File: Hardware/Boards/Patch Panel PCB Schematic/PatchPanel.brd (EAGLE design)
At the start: 226 x 119 mm, 49 parts

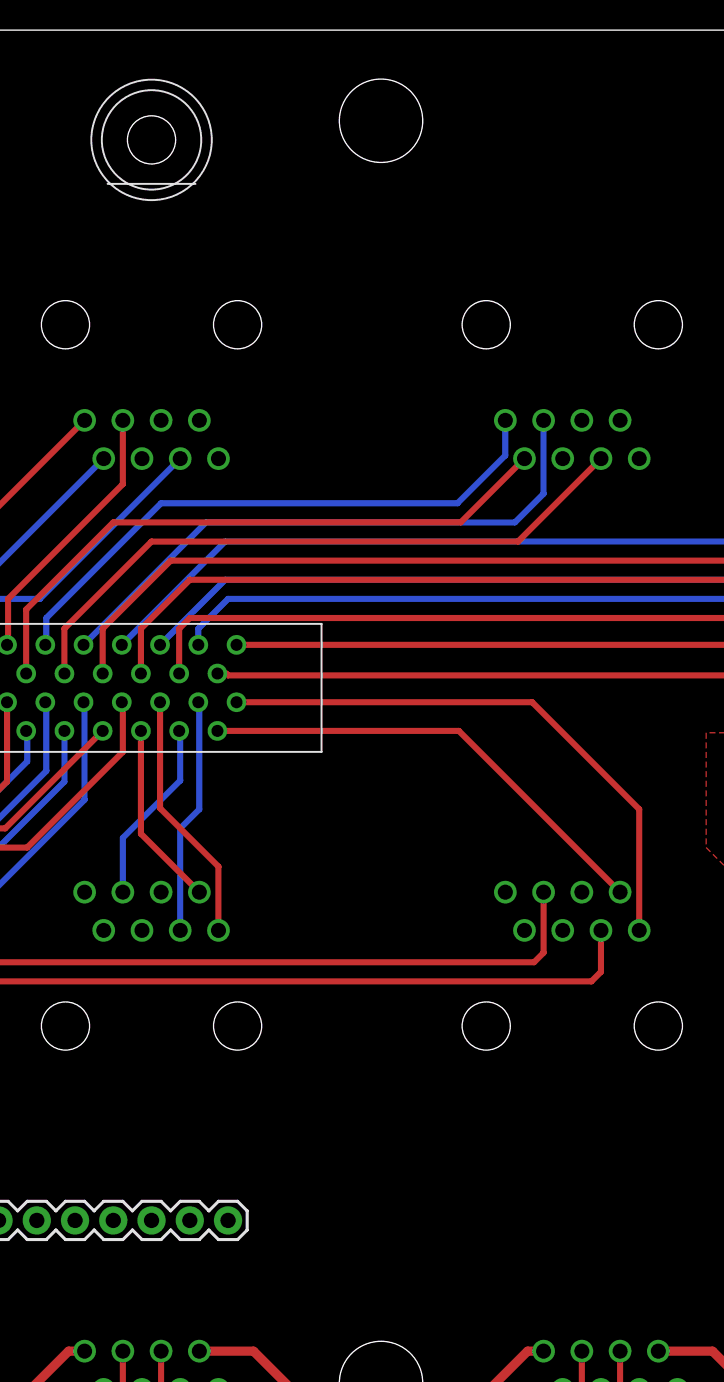
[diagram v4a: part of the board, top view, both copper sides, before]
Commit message: Moved SMA connector
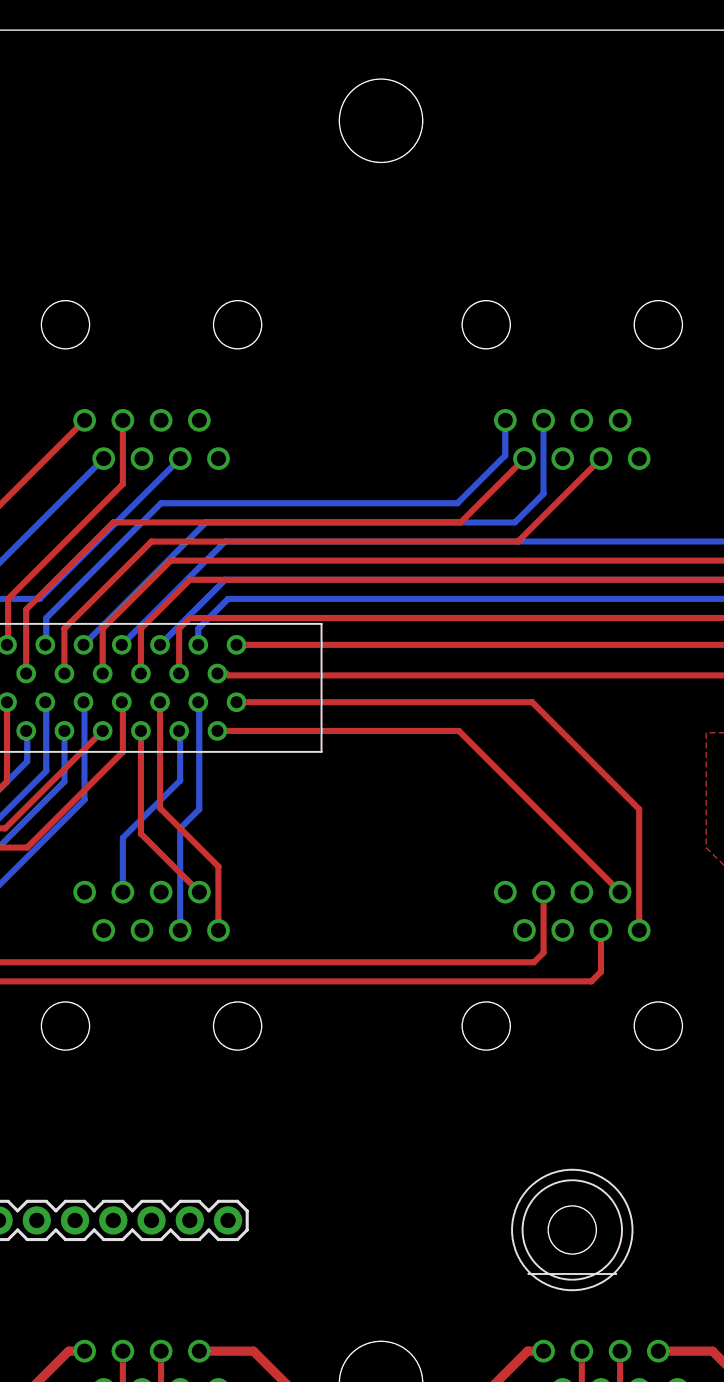
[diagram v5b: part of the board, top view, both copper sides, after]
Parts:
- moved U$16 77.6 mm to (154.9, 39.4)
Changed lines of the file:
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@@
 <element name="U$14" library="ant-pass-through" package="N-TYPE" value="N-TYPE-THRU" x="12.7" y="21.59"/>
 <element name="U$15" library="ant-pass-through" package="N-TYPE" value="N-TYPE-THRU" x="181.61" y="46.99"/>
-<element name="U$16" library="ant-pass-through" package="SMA" value="SMA-THRU" x="127" y="111.76"/>
+<element name="U$16" library="ant-pass-through" package="SMA" value="SMA-THRU" x="154.94" y="39.37"/>
 </elements>
 <signals>

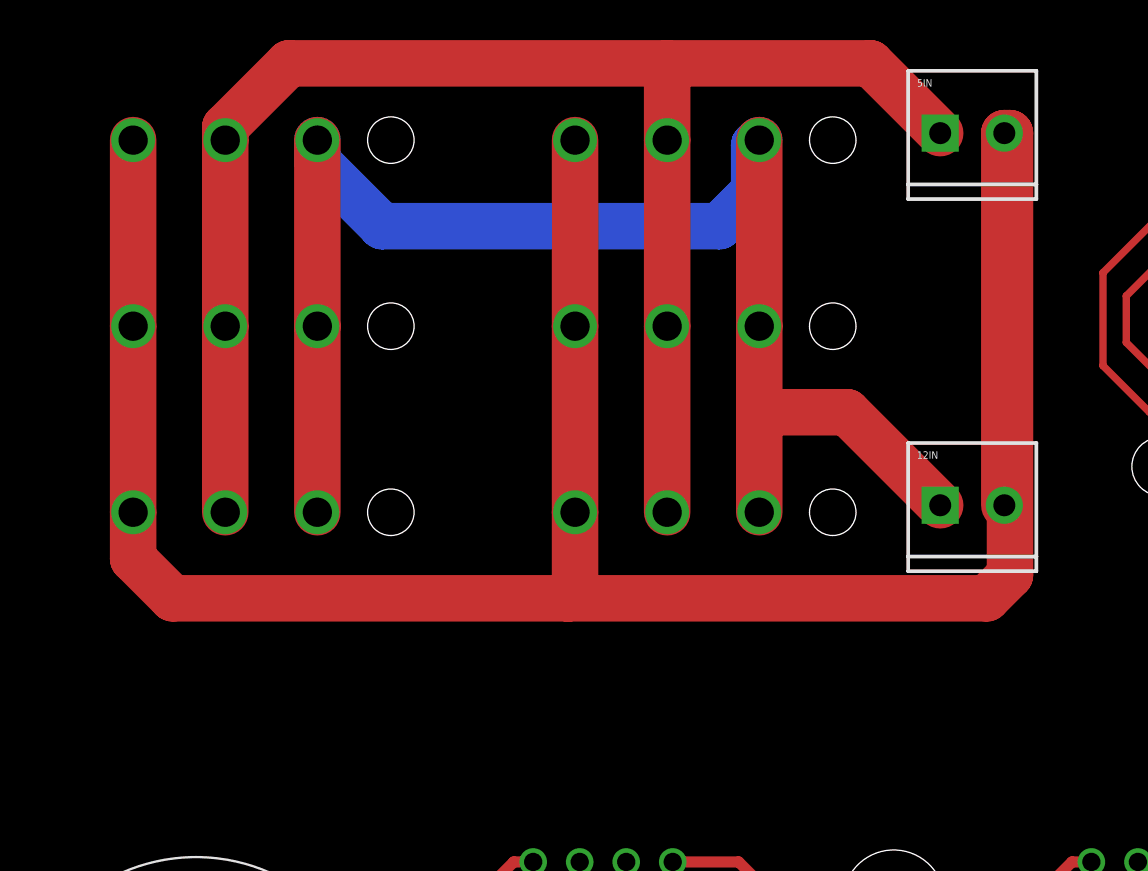
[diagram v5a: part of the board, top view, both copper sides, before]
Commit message: Added space between aux power connectors
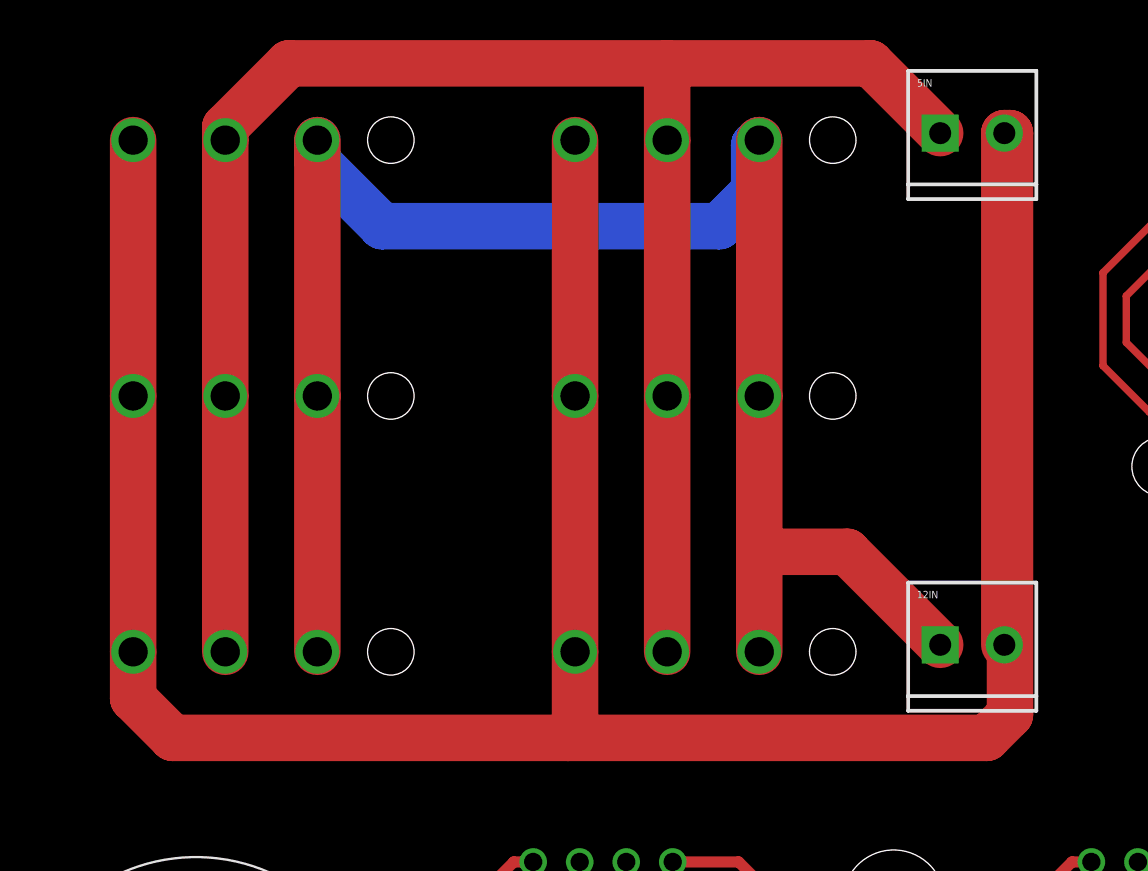
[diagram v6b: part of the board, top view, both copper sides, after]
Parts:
- moved 12IN 7.62 mm to (53.3, 43.2)
- moved U$6 7.62 mm to (5.08, 47.0)
- moved U$7 7.62 mm to (29.2, 47.0)
- moved U$4 3.81 mm to (5.08, 61.0)
- moved U$5 3.81 mm to (29.2, 61.0)
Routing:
- net GND: track 142.1 -> 172.6 mm
- net +5V: track 87.6 -> 102.8 mm
- net +12V: track 82.8 -> 98.0 mm
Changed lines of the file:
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@@
 <element name="RS-485_OUT7" library="PCB0M1" package="RJ45-CAT5E" value="RJ45" x="43.18" y="97.79" rot="MR180"/>
 <element name="U$1" library="harting-scsi" package="60050685100" value="TB60050685100" x="85.09" y="71.12"/>
-<element name="12IN" library="SparkFun-Connectors" package="SCREWTERMINAL-3.5MM-2" value="M023.5MM" x="53.34" y="50.8"/>
+<element name="12IN" library="SparkFun-Connectors" package="SCREWTERMINAL-3.5MM-2" value="M023.5MM" x="53.34" y="43.18"/>
 <element name="5IN" library="SparkFun-Connectors" package="SCREWTERMINAL-3.5MM-2" value="M023.5MM" x="53.34" y="71.12"/>
 <element name="U$2" library="molex-power" package="0.93&quot;" value="3PIN" x="5.08" y="74.93" rot="MR180"/>
 <element name="U$3" library="molex-power" package="0.93&quot;" value="3PIN" x="29.21" y="74.93" rot="MR180"/>
-<element name="U$4" library="molex-power" package="0.93&quot;" value="3PIN" x="5.08" y="64.77" rot="MR180"/>
-<element name="U$5" library="molex-power" package="0.93&quot;" value="3PIN" x="29.21" y="64.77" rot="MR180"/>
-<element name="U$6" library="molex-power" package="0.93&quot;" value="3PIN" x="5.08" y="54.61" rot="MR180"/>
-<element name="U$7" library="molex-power" package="0.93&quot;" value="3PIN" x="29.21" y="54.61" rot="MR180"/>
+<element name="U$4" library="molex-power" package="0.93&quot;" value="3PIN" x="5.08" y="60.96" rot="MR180"/>
+<element name="U$5" library="molex-power" package="0.93&quot;" value="3PIN" x="29.21" y="60.96" rot="MR180"/>
+<element name="U$6" library="molex-power" package="0.93&quot;" value="3PIN" x="5.08" y="46.99" rot="MR180"/>
+<element name="U$7" library="molex-power" package="0.93&quot;" value="3PIN" x="29.21" y="46.99" rot="MR180"/>
 <element name="U$8" library="MLX" package="42002-2" value="MLX-2" x="172.72" y="69.85" rot="MR0"/>
 <element name="U$9" library="MLX" package="42002-2" value="MLX-2" x="194.31" y="64.77" rot="R90"/>
@@
 <contactref element="U$7" pad="3"/>
 <contactref element="U$6" pad="3"/>
-<wire x1="9.271" y1="70.739" x2="9.271" y2="60.579" width="2.54" layer="1"/>
-<wire x1="9.271" y1="60.579" x2="9.271" y2="50.419" width="2.54" layer="1"/>
-<wire x1="33.401" y1="70.739" x2="33.401" y2="60.579" width="2.54" layer="1"/>
-<wire x1="33.401" y1="60.579" x2="33.401" y2="50.419" width="2.54" layer="1"/>
-<wire x1="56.84" y1="50.8" x2="56.84" y2="71.12" width="2.54" layer="1"/>
+<wire x1="9.271" y1="70.739" x2="9.271" y2="56.769" width="2.54" layer="1"/>
+<wire x1="9.271" y1="56.769" x2="9.271" y2="42.799" width="2.54" layer="1"/>
+<wire x1="33.401" y1="70.739" x2="33.401" y2="56.769" width="2.54" layer="1"/>
+<wire x1="33.401" y1="56.769" x2="33.401" y2="42.799" width="2.54" layer="1"/>
+<wire x1="56.84" y1="43.18" x2="56.84" y2="71.12" width="2.54" layer="1"/>
 <wire x1="56.84" y1="71.12" x2="57.15" y2="71.12" width="2.54" layer="1"/>
-<wire x1="57.15" y1="71.12" x2="57.15" y2="46.99" width="2.54" layer="1"/>
-<wire x1="57.15" y1="46.99" x2="55.88" y2="45.72" width="2.54" layer="1"/>
-<wire x1="55.88" y1="45.72" x2="33.02" y2="45.72" width="2.54" layer="1"/>
-<wire x1="11.43" y1="45.72" x2="9.271" y2="47.879" width="2.54" layer="1"/>
-<wire x1="9.271" y1="47.879" x2="9.271" y2="50.419" width="2.54" layer="1"/>
-<wire x1="11.43" y1="45.72" x2="33.02" y2="45.72" width="2.54" layer="1"/>
-<wire x1="33.02" y1="45.72" x2="33.401" y2="46.101" width="2.54" layer="1"/>
-<wire x1="33.401" y1="46.101" x2="33.401" y2="50.419" width="2.54" layer="1"/>
+<wire x1="57.15" y1="71.12" x2="57.15" y2="39.37" width="2.54" layer="1"/>
+<wire x1="57.15" y1="39.37" x2="55.88" y2="38.1" width="2.54" layer="1"/>
+<wire x1="55.88" y1="38.1" x2="33.02" y2="38.1" width="2.54" layer="1"/>
+<wire x1="11.43" y1="38.1" x2="9.271" y2="40.259" width="2.54" layer="1"/>
+<wire x1="9.271" y1="40.259" x2="9.271" y2="42.799" width="2.54" layer="1"/>
+<wire x1="11.43" y1="38.1" x2="33.02" y2="38.1" width="2.54" layer="1"/>
+<wire x1="33.02" y1="38.1" x2="33.401" y2="38.481" width="2.54" layer="1"/>
+<wire x1="33.401" y1="38.481" x2="33.401" y2="42.799" width="2.54" layer="1"/>
 </signal>
 <signal name="+12V">
@@
 <contactref element="U$7" pad="1"/>
 <contactref element="U$6" pad="1"/>
-<wire x1="19.3294" y1="50.419" x2="19.3294" y2="60.579" width="2.54" layer="1"/>
-<wire x1="19.3294" y1="60.579" x2="19.3294" y2="70.739" width="2.54" layer="1"/>
-<wire x1="43.4594" y1="70.739" x2="43.4594" y2="60.579" width="2.54" layer="1"/>
-<wire x1="43.4594" y1="50.419" x2="43.4594" y2="55.88" width="2.54" layer="1"/>
-<wire x1="43.4594" y1="55.88" x2="43.4594" y2="60.579" width="2.54" layer="1"/>
+<wire x1="19.3294" y1="42.799" x2="19.3294" y2="56.769" width="2.54" layer="1"/>
+<wire x1="19.3294" y1="56.769" x2="19.3294" y2="70.739" width="2.54" layer="1"/>
+<wire x1="43.4594" y1="70.739" x2="43.4594" y2="56.769" width="2.54" layer="1"/>
+<wire x1="43.4594" y1="42.799" x2="43.4594" y2="48.26" width="2.54" layer="1"/>
+<wire x1="43.4594" y1="48.26" x2="43.4594" y2="56.769" width="2.54" layer="1"/>
 <wire x1="43.4594" y1="70.739" x2="43.18" y2="70.4596" width="2.54" layer="16"/>
 <wire x1="43.18" y1="70.4596" x2="43.18" y2="67.945" width="2.54" layer="16"/>
@@
 <wire x1="22.86" y1="66.04" x2="19.3294" y2="69.5706" width="2.54" layer="16"/>
 <wire x1="19.3294" y1="69.5706" x2="19.3294" y2="70.739" width="2.54" layer="16"/>
-<wire x1="53.34" y1="50.8" x2="48.26" y2="55.88" width="2.54" layer="1"/>
-<wire x1="48.26" y1="55.88" x2="43.4594" y2="55.88" width="2.54" layer="1"/>
+<wire x1="53.34" y1="43.18" x2="48.26" y2="48.26" width="2.54" layer="1"/>
+<wire x1="48.26" y1="48.26" x2="43.4594" y2="48.26" width="2.54" layer="1"/>
 </signal>
 <signal name="+5V">
@@
 <contactref element="U$7" pad="2"/>
 <contactref element="U$6" pad="2"/>
-<wire x1="14.3002" y1="70.739" x2="14.3002" y2="60.579" width="2.54" layer="1"/>
-<wire x1="14.3002" y1="60.579" x2="14.3002" y2="50.419" width="2.54" layer="1"/>
-<wire x1="38.4302" y1="70.739" x2="38.4302" y2="60.579" width="2.54" layer="1"/>
-<wire x1="38.4302" y1="60.579" x2="38.4302" y2="50.419" width="2.54" layer="1"/>
+<wire x1="14.3002" y1="70.739" x2="14.3002" y2="56.769" width="2.54" layer="1"/>
+<wire x1="14.3002" y1="56.769" x2="14.3002" y2="42.799" width="2.54" layer="1"/>
+<wire x1="38.4302" y1="70.739" x2="38.4302" y2="56.769" width="2.54" layer="1"/>
+<wire x1="38.4302" y1="56.769" x2="38.4302" y2="42.799" width="2.54" layer="1"/>
 <wire x1="53.34" y1="71.12" x2="49.53" y2="74.93" width="2.54" layer="1"/>
 <wire x1="38.4302" y1="74.93" x2="17.78" y2="74.93" width="2.54" layer="1"/>
